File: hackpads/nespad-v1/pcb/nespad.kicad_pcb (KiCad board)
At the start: 2 copper layers, 85.7 x 66.7 mm, 7 parts, among them SW1 SW_Push, SW2 SW_Push, SW3 SW_Push, SW4 SW_Push, SW5 SW_Push, SW6 SW_Push, U1 XIAO-RP2040-DIP

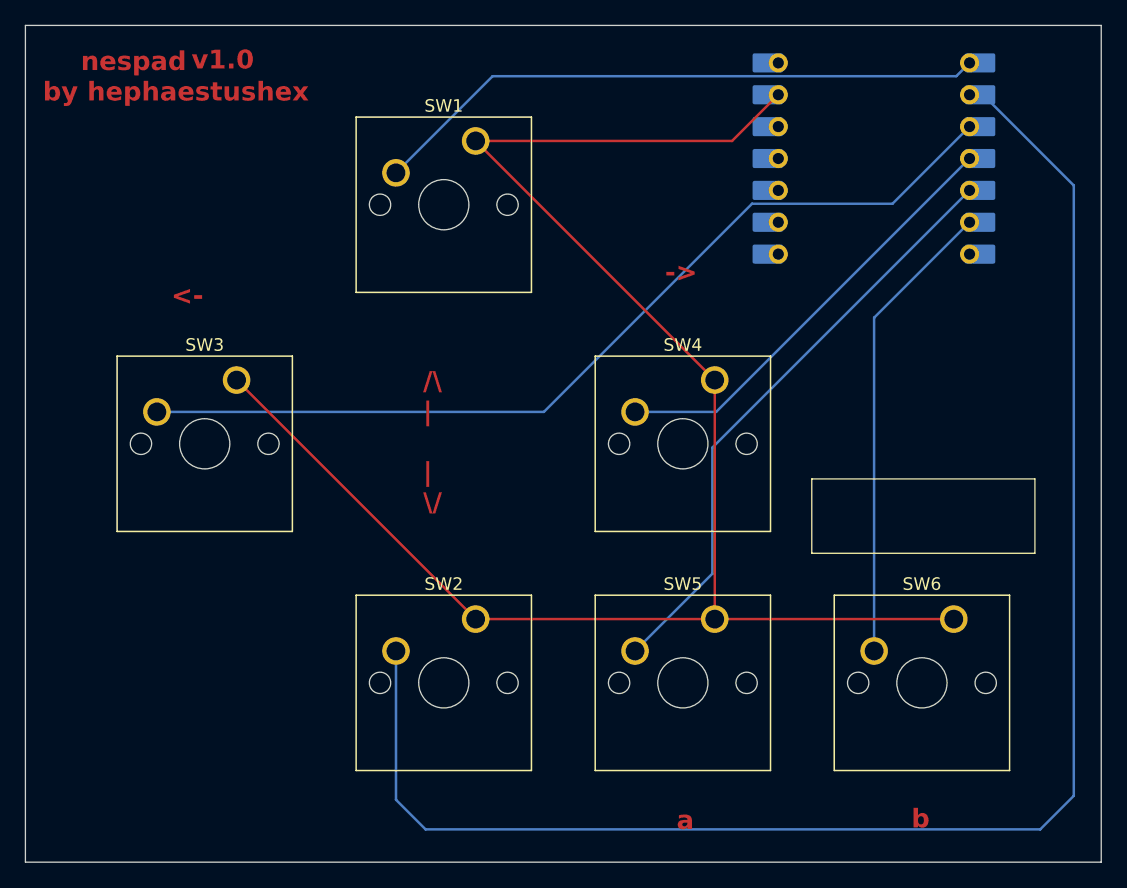
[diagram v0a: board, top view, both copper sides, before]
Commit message: Moved art from copper to silkscreen
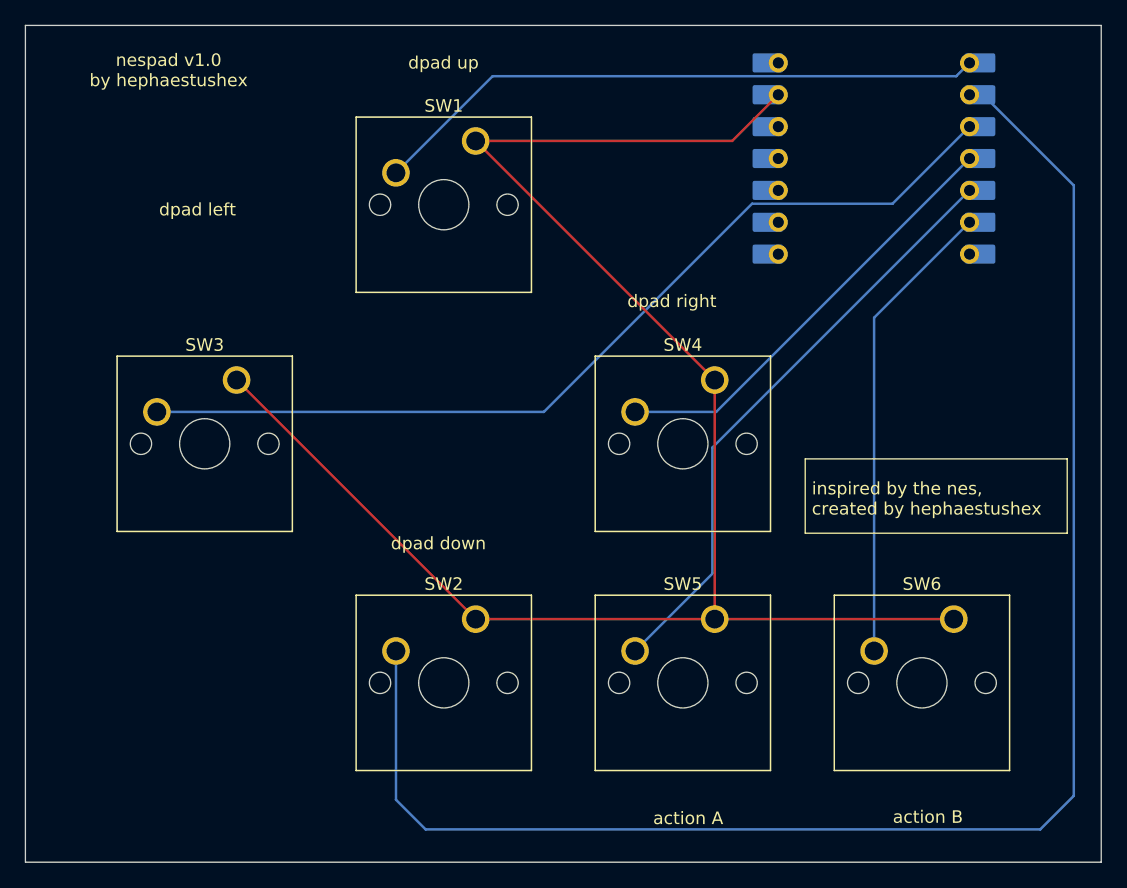
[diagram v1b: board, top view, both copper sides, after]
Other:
- board text added: "action A"
- board text added: "action B"
- board text added: "dpad down"
- board text added: "dpad left"
- board text added: "dpad right"
- board text added: "dpad up"
- board text added: "inspired by the nes, created by hephaestushex"
- board text added: "nespad v1.0 by hephaestushex"
- board text removed: "->"
- board text removed: "/\ | | \/"
- board text removed: "<-"
- board text removed: "a"
- board text removed: "b"
- board text removed: "by hephaestushex"
- board text removed: "nespad"
- board text removed: "v1.0"
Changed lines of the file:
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@@
 			(outputformat 1)
 			(mirror no)
-			(drillshape 1)
+			(drillshape 0)
 			(scaleselection 1)
-			(outputdirectory "")
+			(outputdirectory "C:/Users/shrav/Documents/hackpad/hackpads/nespad-v1/production/gerbers/")
 		)
 	)
@@
 	)
 	(gr_rect
-		(start 146.465 102.01)
-		(end 164.24 107.935)
+		(start 145.94 100.41)
+		(end 166.815 106.335)
 		(stroke
 			(width 0.1)
@@
 		(layer "Edge.Cuts")
 	)
-	(gr_text "by hephaestushex"
-		(at 85.19 72.035 0)
-		(layer "F.Cu")
+	(gr_text "dpad left"
+		(at 97.515 81.135 0)
+		(layer "F.SilkS")
 		(effects
 			(font
-				(size 1.5 1.5)
-				(thickness 0.3)
-				(bold yes)
-			)
-			(justify left bottom)
+				(size 1 1)
+				(thickness 0.1)
+			)
+			(justify bottom)
 		)
 	)
-	(gr_text "<-"
-		(at 95.415 88.285 0)
-		(layer "F.Cu")
+	(gr_text "dpad up"
+		(at 117.115 69.435 0)
+		(layer "F.SilkS")
 		(effects
 			(font
-				(size 1.5 1.5)
-				(thickness 0.3)
-				(bold yes)
-			)
-			(justify left bottom)
+				(size 1 1)
+				(thickness 0.1)
+			)
+			(justify bottom)
 		)
 	)
-	(gr_text "->"
-		(at 134.765 86.435 0)
-		(layer "F.Cu")
+	(gr_text "nespad v1.0\nby hephaestushex"
+		(at 95.215 70.835 0)
+		(layer "F.SilkS")
 		(effects
 			(font
-				(size 1.5 1.5)
-				(thickness 0.3)
-				(bold yes)
-			)
-			(justify left bottom)
+				(size 1 1)
+				(thickness 0.1)
+			)
+			(justify bottom)
 		)
 	)
-	(gr_text "nespad"
-		(at 88.215 69.61 0)
-		(layer "F.Cu")
+	(gr_text "dpad right"
+		(at 135.315 88.435 0)
+		(layer "F.SilkS")
 		(effects
 			(font
-				(size 1.5 1.5)
-				(thickness 0.3)
-				(bold yes)
-			)
-			(justify left bottom)
+				(size 1 1)
+				(thickness 0.1)
+			)
+			(justify bottom)
 		)
 	)
-	(gr_text "b"
-		(at 154.39 129.96 0)
-		(layer "F.Cu")
+	(gr_text "action B"
+		(at 155.715 129.535 0)
+		(layer "F.SilkS")
 		(effects
 			(font
-				(size 1.5 1.5)
-				(thickness 0.3)
-				(bold yes)
-			)
-			(justify left bottom)
+				(size 1 1)
+				(thickness 0.1)
+			)
+			(justify bottom)
 		)
 	)
-	(gr_text "/\\\n|\n\n|\n\\/"
-		(at 115.49 104.76 0)
-		(layer "F.Cu")
+	(gr_text "action A"
+		(at 136.615 129.635 0)
+		(layer "F.SilkS")
 		(effects
 			(font
-				(size 1.5 1.5)
-				(thickness 0.3)
-				(bold yes)
-			)
-			(justify left bottom)
+				(size 1 1)
+				(thickness 0.1)
+			)
+			(justify bottom)
 		)
 	)
-	(gr_text "v1.0"
-		(at 97.04 69.485 0)
-		(layer "F.Cu")
+	(gr_text "dpad down"
+		(at 116.715 107.735 0)
+		(layer "F.SilkS")
 		(effects
 			(font
-				(size 1.5 1.5)
-				(thickness 0.3)
-				(bold yes)
-			)
-			(justify left bottom)
+				(size 1 1)
+				(thickness 0.1)
+			)
+			(justify bottom)
 		)
 	)
-	(gr_text "a"
-		(at 135.69 130.085 0)
-		(layer "F.Cu")
+	(gr_text "inspired by the nes,\ncreated by hephaestushex"
+		(at 146.465 104.9725 0)
+		(layer "F.SilkS")
 		(effects
 			(font
-				(size 1.5 1.5)
-				(thickness 0.3)
-				(bold yes)
+				(size 1 1)
+				(thickness 0.1)
 			)
 			(justify left bottom)
